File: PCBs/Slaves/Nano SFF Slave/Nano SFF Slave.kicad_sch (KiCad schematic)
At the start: 66 parts, among them J1 Screw_Terminal_01x02, J10 AVR-ISP-6, J11 Conn_01x06_Female, J12 Screw_Terminal_01x02, J13 Screw_Terminal_01x02, J14 Screw_Terminal_01x02, J15 Screw_Terminal_01x02, J16 Screw_Terminal_01x02, J2 Screw_Terminal_01x02, J3 Screw_Terminal_01x02, J4 Screw_Terminal_01x02, J5 Screw_Terminal_01x02, J6 Screw_Terminal_01x02, J7 Screw_Terminal_01x02, J8 Screw_Terminal_01x02, J9 Screw_Terminal_01x02, SW1 SW_DIP_x02, SW2 SW_DIP_x02, SW3 SW_MEC_5E, U1 ATmega328P-AU, U10 TISP4240M3BJR-S, U2 MAX487ESA+T, U3 ULN2003A, U4 MAX487CPA+, U5 AMS1117-5.0, U6 HY15P03C2, U7 TBU-CA065-200-WH, U8 TBU-CA065-200-WH, U9 TISP4240M3BJR-S, Y1 Crystal_GND24

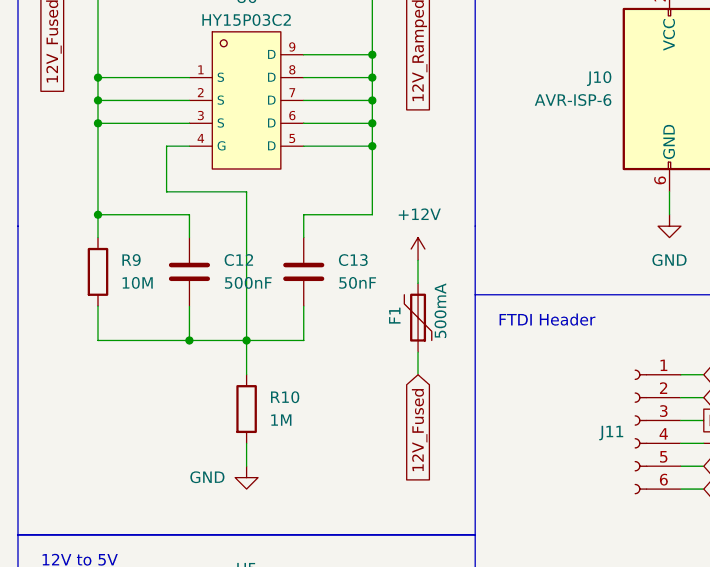
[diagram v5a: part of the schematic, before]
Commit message: Updated LCSC number and size of voltage ramp capacitors for Nano SFF Slave
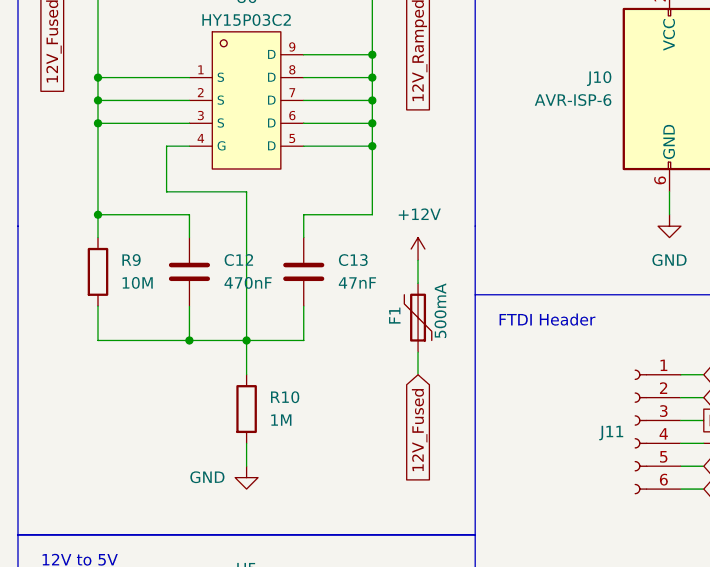
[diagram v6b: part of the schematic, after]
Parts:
- C12: value 500nF -> 470nF; footprint A10 KiCad Libraries:C0402 -> Capacitor_SMD:C_0603_1608Metric; LCSC TBA -> C1623
- C13: value 50nF -> 47nF; footprint A10 KiCad Libraries:C0402 -> Capacitor_SMD:C_0603_1608Metric; LCSC TBA -> C1622
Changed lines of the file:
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@@
       (effects (font (size 1.27 1.27)) (justify left))
     )
-    (property "Value" "50nF" (id 1) (at 48.26 95.2499 0)
-      (effects (font (size 1.27 1.27)) (justify left))
-    )
-    (property "Footprint" "A10 KiCad Libraries:C0402" (id 2) (at 45.4152 97.79 0)
+    (property "Value" "47nF" (id 1) (at 48.26 95.2499 0)
+      (effects (font (size 1.27 1.27)) (justify left))
+    )
+    (property "Footprint" "Capacitor_SMD:C_0603_1608Metric" (id 2) (at 45.4152 97.79 0)
       (effects (font (size 1.27 1.27)) hide)
     )
@@
       (effects (font (size 1.27 1.27)) hide)
     )
-    (property "LCSC" "TBA" (id 4) (at 44.45 93.98 0)
+    (property "LCSC" "C1622" (id 4) (at 44.45 93.98 0)
       (effects (font (size 1.27 1.27)) hide)
     )
@@
       (effects (font (size 1.27 1.27)) (justify left))
     )
-    (property "Value" "500nF" (id 1) (at 35.56 95.2499 0)
-      (effects (font (size 1.27 1.27)) (justify left))
-    )
-    (property "Footprint" "A10 KiCad Libraries:C0402" (id 2) (at 32.7152 97.79 0)
+    (property "Value" "470nF" (id 1) (at 35.56 95.2499 0)
+      (effects (font (size 1.27 1.27)) (justify left))
+    )
+    (property "Footprint" "Capacitor_SMD:C_0603_1608Metric" (id 2) (at 32.7152 97.79 0)
       (effects (font (size 1.27 1.27)) hide)
     )
@@
       (effects (font (size 1.27 1.27)) hide)
     )
-    (property "LCSC" "TBA" (id 4) (at 31.75 93.98 0)
+    (property "LCSC" "C1623" (id 4) (at 31.75 93.98 0)
       (effects (font (size 1.27 1.27)) hide)
     )
@@
     )
     (path "/dbc5fd48-5195-4b41-be0e-503a8df5dd8e"
-      (reference "C12") (unit 1) (value "500nF") (footprint "A10 KiCad Libraries:C0402")
+      (reference "C12") (unit 1) (value "470nF") (footprint "Capacitor_SMD:C_0603_1608Metric")
     )
     (path "/6e1cc3a1-d156-439d-9e01-aa13697bc266"
-      (reference "C13") (unit 1) (value "50nF") (footprint "A10 KiCad Libraries:C0402")
+      (reference "C13") (unit 1) (value "47nF") (footprint "Capacitor_SMD:C_0603_1608Metric")
     )
     (path "/294162e1-5bbc-43c1-8530-fdc705d0d68f"

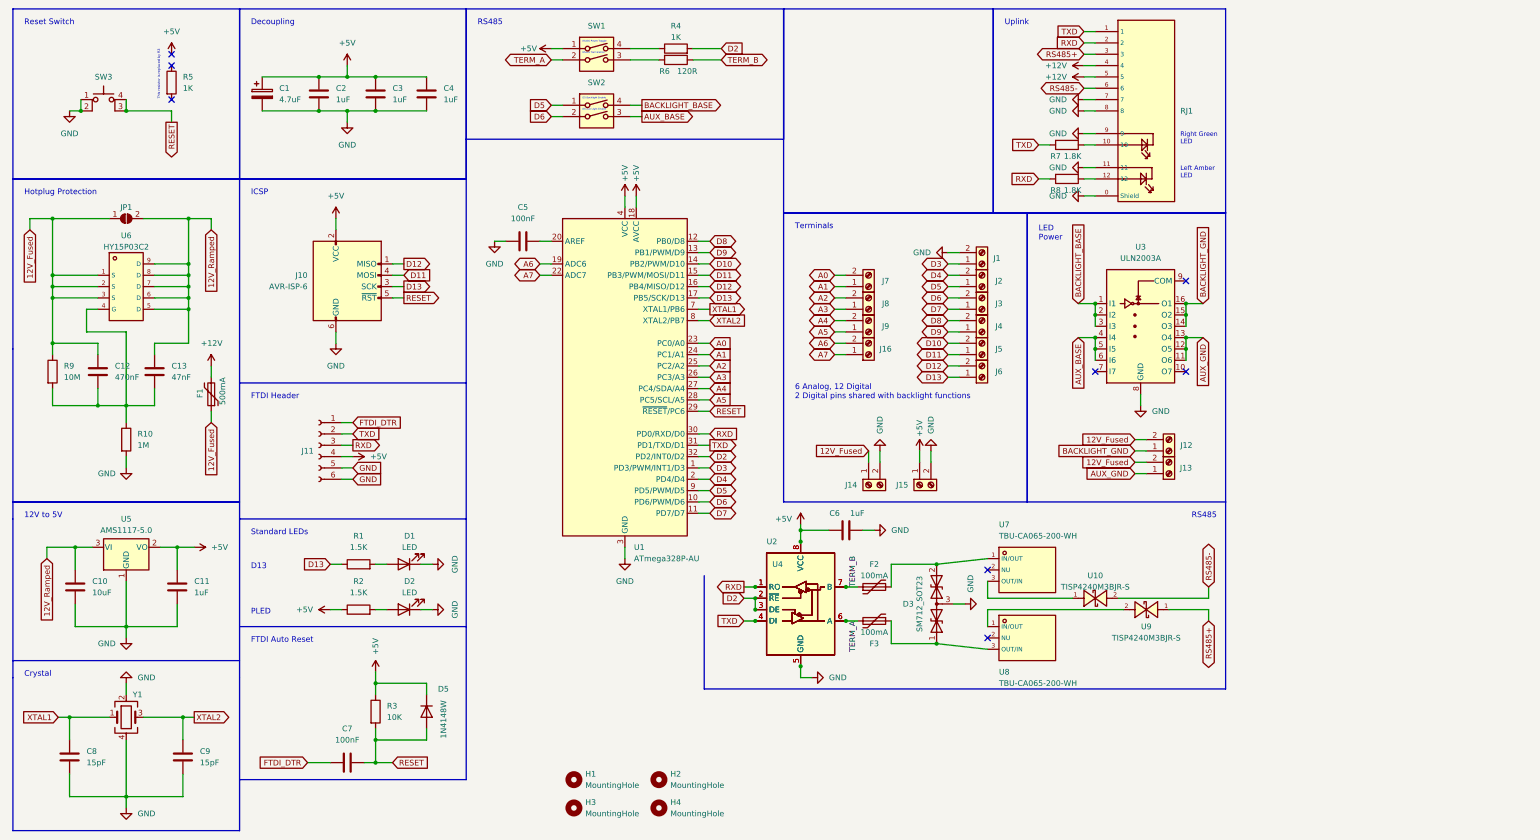
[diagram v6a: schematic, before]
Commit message: Removed voltage ramp and some protection from Nano SFF Slave
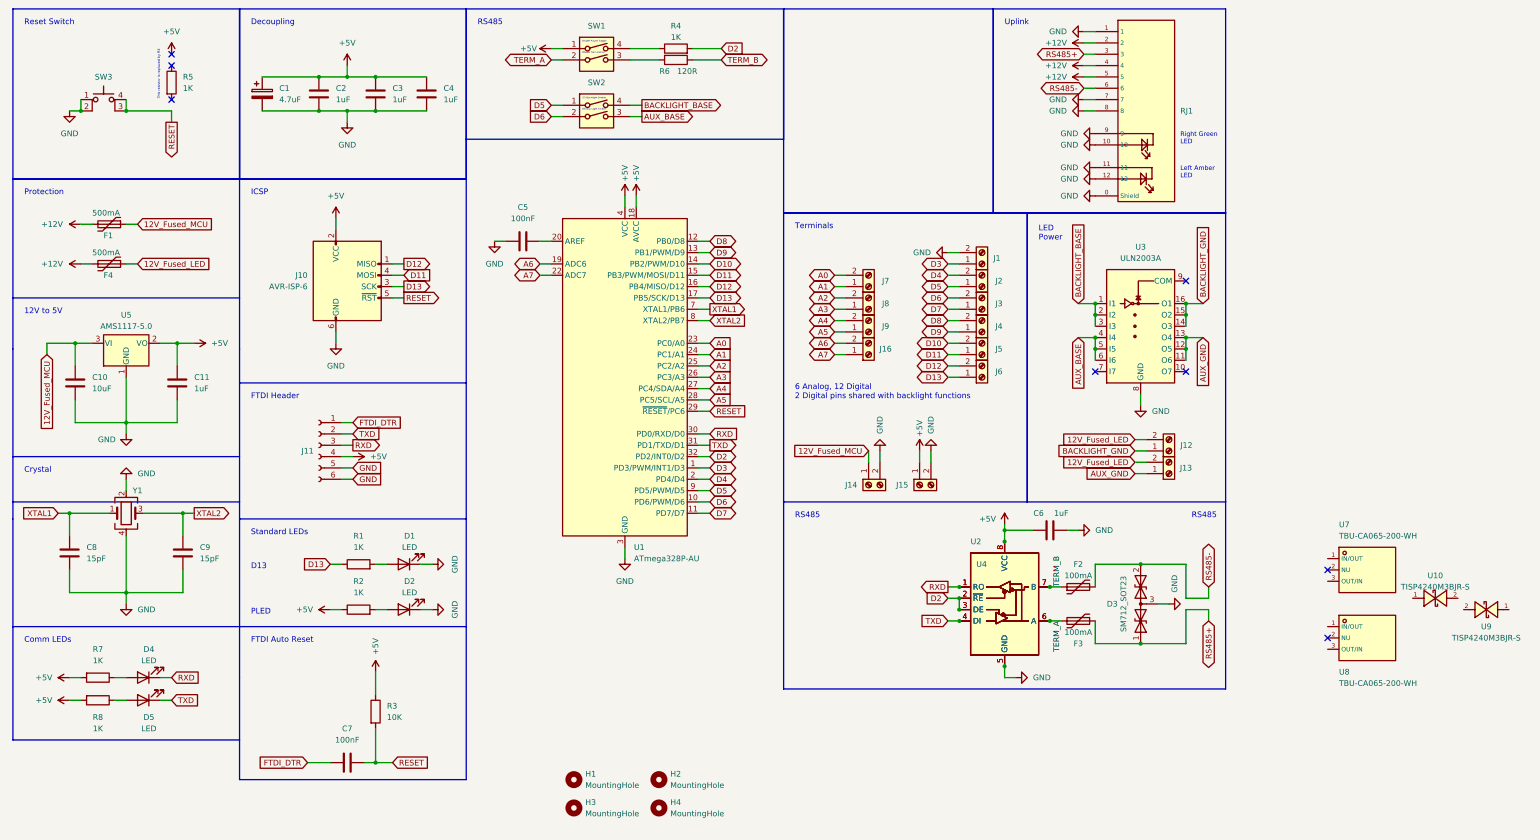
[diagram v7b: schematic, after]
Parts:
- removed C12: 470nF, Capacitor_SMD:C_0603_1608Metric, symbol Device:C
- removed C13: 47nF, Capacitor_SMD:C_0603_1608Metric, symbol Device:C
- removed D5: 1N4148W, Diode_SMD:D_SOD-123, symbol Device:D
- removed JP1: Solder, Jumper:SolderJumper-2_P1.3mm_Open_RoundedPad1.0x1.5mm, symbol Jumper:SolderJumper_2_Open
- removed R10: 1M, Resistor_SMD:R_0603_1608Metric, symbol Device:R
- removed R9: 10M, Resistor_SMD:R_0603_1608Metric, symbol Device:R
- removed U6: HY15P03C2, A10 KiCad Libraries:DFN-8_L5.9-W5.2-P1.27-LS6.2-BL, symbol A10:HY15P03C2
- added D4, D5: LED, LED_SMD:LED_0603_1608Metric, symbol Device:LED
- added F4: 500mA, Fuse:Fuse_1206_3216Metric, symbol Device:Polyfuse
- R1, R2: value 1.5K -> 1K; footprint Resistor_SMD:R_0805_2012Metric -> Resistor_SMD:R_0402_1005Metric; LCSC C4310 -> C11702
- R4: footprint Resistor_SMD:R_0805_2012Metric -> Resistor_SMD:R_0402_1005Metric; LCSC C17513 -> C11702
- R7, R8: value 1.8K -> 1K; footprint Resistor_SMD:R_0805_2012Metric -> Resistor_SMD:R_0402_1005Metric; LCSC C17398 -> C11702
- U10, U7, U8, U9: now left out of the parts list
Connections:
- net +12V: now also RJ1.2, F4.2
- net +5V: now also R7.2, R8.2
- net GND: now also RJ1.1, RJ1.10, RJ1.12
- net RS485+: now also D3.1 (A1), F3.1; no longer U9.1 (A)
- net RS485-: now also D3.2 (A2), F2.2; no longer U10.2 (K)
- net RXD: now also D4.1 (K); no longer R8.2, RJ1.2
- net TXD: now also D5.1 (K); no longer R7.2, RJ1.1
- net at U9.2 (K): no longer U8.1 (IN/OUT)
- net at U10.1 (A): no longer U7.3 (OUT/IN)
- net at R7.1: now also D4.2 (A); no longer RJ1.10
- net at R8.1: now also D5.2 (A); no longer RJ1.12
- net 12V_Fused renamed 12V_Fused_LED
- net 12V_Fused_LED: now also F4.1; no longer F1.1, J14.1 (Pin_1)
- net 12V_Ramped renamed 12V_Fused_MCU
- net 12V_Fused_MCU: now also F1.1, J14.1 (Pin_1)
- now unconnected: U7.1 (IN/OUT), U8.3 (OUT/IN)
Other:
- note added: "Comm LEDs"
- note added: "Protection"
- note removed: "Hotplug Protection"
- moved on the sheet: C10, C11, C6, C8, C9, D3, F1, F2, F3, U10, U2, U4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

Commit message: Updated Nano SFF Slave
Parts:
- added R10: 3.6K, Resistor_SMD:R_0603_1608Metric, symbol Device:R
- added R9: 1K, Resistor_SMD:R_0402_1005Metric, symbol Device:R
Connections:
- net +5V: now also R9.1
- net 12V_Fused_MCU: now also R10.1
- net GND: no longer RJ1.10, RJ1.12
- new net: R9.2, RJ1.10
- new net: R10.2, RJ1.12
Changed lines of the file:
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@@
     (stroke (width 0) (type default) (color 0 0 0 0))
   )
+  (wire (pts (xy 236.22 50.8) (xy 245.11 50.8))
+    (stroke (width 0) (type default) (color 0 0 0 0))
+  )
   (wire (pts (xy 196.85 82.55) (xy 199.39 82.55))
     (stroke (width 0) (type default) (color 0 0 0 0))
@@
     (stroke (width 0) (type default) (color 0 0 0 0))
   )
+  (wire (pts (xy 252.73 50.8) (xy 255.27 50.8))
+    (stroke (width 0) (type default) (color 0 0 0 0))
+  )
   (wire (pts (xy 25.4 125.73) (xy 25.4 130.81))
     (stroke (width 0) (type default) (color 0 0 0 0))
@@
     (stroke (width 0) (type default) (color 0 0 0 0))
   )
+  (wire (pts (xy 242.57 43.18) (xy 245.11 43.18))
+    (stroke (width 0) (type default) (color 0 0 0 0))
+  )
   (wire (pts (xy 222.25 149.86) (xy 224.79 149.86))
     (stroke (width 0) (type default) (color 0 0 0 0))
@@
     (stroke (width 0) (type default) (color 0 0 0 0))
   )
+  (wire (pts (xy 252.73 43.18) (xy 255.27 43.18))
+    (stroke (width 0) (type default) (color 0 0 0 0))
+  )
   (wire (pts (xy 38.1 33.02) (xy 38.1 35.56))
     (stroke (width 0) (type default) (color 0 0 0 0))
@@
     )
   )
+  (global_label "12V_Fused_MCU" (shape input) (at 236.22 50.8 90) (fields_autoplaced)
+    (effects (font (size 1.27 1.27)) (justify left))
+    (property "Intersheet References" "${INTERSHEET_REFS}" (id 0) (at 236.2994 33.3888 90)
+      (effects (font (size 1.27 1.27)) (justify left) hide)
+    )
+  )
   (global_label "12V_Fused_LED" (shape input) (at 264.16 109.22 180) (fields_autoplaced)
     (effects (font (size 1.27 1.27)) (justify right))
@@
   )
   (symbol (lib_id "power:GND") (at 255.27 54.61 270) (unit 1)
-    (in_bom yes) (on_board yes) (fields_autoplaced)
+    (in_bom yes) (on_board yes)
     (property "Reference" "#PWR0118" (id 0) (at 248.92 54.61 0)
       (effects (font (size 1.27 1.27)) hide)
     )
-    (property "Value" "GND" (id 1) (at 251.46 54.6099 90)
+    (property "Value" "GND" (id 1) (at 251.46 55.88 90)
       (effects (font (size 1.27 1.27)) (justify right))
     )
@@
   (symbol (lib_id "power:GND") (at 255.27 40.64 270) (unit 1)
     (in_bom yes) (on_board yes) (fields_autoplaced)
-    (property "Reference" "#PWR?" (id 0) (at 248.92 40.64 0)
+    (property "Reference" "#PWR0121" (id 0) (at 248.92 40.64 0)
       (effects (font (size 1.27 1.27)) hide)
     )
@@
     (pin "1")
   )
+  (symbol (lib_id "Device:R") (at 248.92 43.18 90) (unit 1)
+    (in_bom yes) (on_board yes)
+    (property "Reference" "R9" (id 0) (at 246.38 45.72 90))
+    (property "Value" "1K" (id 1) (at 251.46 45.72 90))
+    (property "Footprint" "Resistor_SMD:R_0402_1005Metric" (id 2) (at 248.92 44.958 90)
+      (effects (font (size 1.27 1.27)) hide)
+    )
+    (property "Datasheet" "~" (id 3) (at 248.92 43.18 0)
+      (effects (font (size 1.27 1.27)) hide)
+    )
+    (property "LCSC" "C11702" (id 4) (at 248.92 43.18 0)
+      (effects (font (size 1.27 1.27)) hide)
+    )
+    (pin "1")
+    (pin "2")
+  )
   (symbol (lib_id "Connector:Screw_Terminal_01x02") (at 229.87 90.17 0) (mirror x) (unit 1)
     (in_bom yes) (on_board yes)
@@
   (symbol (lib_id "power:GND") (at 255.27 48.26 270) (unit 1)
     (in_bom yes) (on_board yes) (fields_autoplaced)
-    (property "Reference" "#PWR?" (id 0) (at 248.92 48.26 0)
+    (property "Reference" "#PWR0130" (id 0) (at 248.92 48.26 0)
       (effects (font (size 1.27 1.27)) hide)
     )
@@
     (pin "2")
   )
-  (symbol (lib_id "power:GND") (at 255.27 50.8 270) (unit 1)
-    (in_bom yes) (on_board yes) (fields_autoplaced)
-    (property "Reference" "#PWR?" (id 0) (at 248.92 50.8 0)
-      (effects (font (size 1.27 1.27)) hide)
-    )
-    (property "Value" "GND" (id 1) (at 251.46 50.7999 90)
-      (effects (font (size 1.27 1.27)) (justify right))
-    )
-    (property "Footprint" "" (id 2) (at 255.27 50.8 0)
-      (effects (font (size 1.27 1.27)) hide)
-    )
-    (property "Datasheet" "" (id 3) (at 255.27 50.8 0)
-      (effects (font (size 1.27 1.27)) hide)
-    )
-    (pin "1")
-  )
   (symbol (lib_id "power:GND") (at 85.09 87.63 0) (unit 1)
     (in_bom yes) (on_board yes)
@@
     (pin "1")
   )
-  (symbol (lib_id "power:GND") (at 255.27 43.18 270) (unit 1)
-    (in_bom yes) (on_board yes) (fields_autoplaced)
-    (property "Reference" "#PWR?" (id 0) (at 248.92 43.18 0)
+  (symbol (lib_id "Device:R") (at 248.92 50.8 90) (unit 1)
+    (in_bom yes) (on_board yes)
+    (property "Reference" "R10" (id 0) (at 246.38 53.34 90))
+    (property "Value" "3.6K" (id 1) (at 251.46 53.34 90))
+    (property "Footprint" "Resistor_SMD:R_0603_1608Metric" (id 2) (at 248.92 52.578 90)
       (effects (font (size 1.27 1.27)) hide)
     )
-    (property "Value" "GND" (id 1) (at 251.46 43.1799 90)
-      (effects (font (size 1.27 1.27)) (justify right))
-    )
-    (property "Footprint" "" (id 2) (at 255.27 43.18 0)
+    (property "Datasheet" "~" (id 3) (at 248.92 50.8 0)
       (effects (font (size 1.27 1.27)) hide)
     )
-    (property "Datasheet" "" (id 3) (at 255.27 43.18 0)
+    (property "LCSC" "C22980" (id 4) (at 248.92 50.8 0)
       (effects (font (size 1.27 1.27)) hide)
     )
     (pin "1")
+    (pin "2")
   )
   (symbol (lib_id "power:+5V") (at 93.98 161.29 0) (unit 1)
@@
     (pin "4")
   )
+  (symbol (lib_id "power:+5V") (at 242.57 43.18 90) (unit 1)
+    (in_bom yes) (on_board yes)
+    (property "Reference" "#PWR0126" (id 0) (at 246.38 43.18 0)
+      (effects (font (size 1.27 1.27)) hide)
+    )
+    (property "Value" "+5V" (id 1) (at 243.84 45.72 90)
+      (effects (font (size 1.27 1.27)) (justify left))
+    )
+    (property "Footprint" "" (id 2) (at 242.57 43.18 0)
+      (effects (font (size 1.27 1.27)) hide)
+    )
+    (property "Datasheet" "" (id 3) (at 242.57 43.18 0)
+      (effects (font (size 1.27 1.27)) hide)
+    )
+    (pin "1")
+  )
   (symbol (lib_id "Connector:Screw_Terminal_01x02") (at 215.9 119.38 90) (mirror x) (unit 1)
     (in_bom yes) (on_board yes)
@@
       (reference "#PWR0120") (unit 1) (value "GND") (footprint "")
     )
+    (path "/4a0c185c-d332-4d31-a687-f91324a5a494"
+      (reference "#PWR0121") (unit 1) (value "GND") (footprint "")
+    )
     (path "/e70032e1-593f-4b8c-9b9c-ad55a3745622"
       (reference "#PWR0122") (unit 1) (value "GND") (footprint "")
@@
       (reference "#PWR0125") (unit 1) (value "+5V") (footprint "")
     )
+    (path "/f12cc227-a1c5-4cc6-bc92-a3276fd7ae08"
+      (reference "#PWR0126") (unit 1) (value "+5V") (footprint "")
+    )
     (path "/8537ef08-22e1-4eec-a09a-d58a3e6da0d2"
       (reference "#PWR0127") (unit 1) (value "+5V") (footprint "")
@@
       (reference "#PWR0129") (unit 1) (value "GND") (footprint "")
     )
+    (path "/6f4643bb-52e5-447e-8449-b8bc3d86b2e0"
+      (reference "#PWR0130") (unit 1) (value "GND") (footprint "")
+    )
     (path "/a94de019-f56e-4619-9189-74d5a7cc128f"
       (reference "#PWR0131") (unit 1) (value "+12V") (footprint "")
@@
       (reference "#PWR0145") (unit 1) (value "+5V") (footprint "")
     )
-    (path "/4a0c185c-d332-4d31-a687-f91324a5a494"
-      (reference "#PWR?") (unit 1) (value "GND") (footprint "")
-    )
-    (path "/6f4643bb-52e5-447e-8449-b8bc3d86b2e0"
-      (reference "#PWR?") (unit 1) (value "GND") (footprint "")
-    )
-    (path "/c16051de-397b-43f7-8128-62b490be7cfc"
-      (reference "#PWR?") (unit 1) (value "GND") (footprint "")
-    )
-    (path "/d054fe41-3500-4ef5-9852-f7fb7b1bea14"
-      (reference "#PWR?") (unit 1) (value "GND") (footprint "")
-    )
     (path "/df5accf7-095f-40f9-b40a-a9b9e4c1a11a"
       (reference "C1") (unit 1) (value "4.7uF") (footprint "A10 KiCad Libraries:C0805")
@@
       (reference "R8") (unit 1) (value "1K") (footprint "Resistor_SMD:R_0402_1005Metric")
     )
+    (path "/67afc716-6f62-4185-8366-23dd26605e5b"
+      (reference "R9") (unit 1) (value "1K") (footprint "Resistor_SMD:R_0402_1005Metric")
+    )
+    (path "/cef69c45-d1b9-4ad8-a826-d9e3e591eaf5"
+      (reference "R10") (unit 1) (value "3.6K") (footprint "Resistor_SMD:R_0603_1608Metric")
+    )
     (path "/b0d080a8-fb27-4ca9-906d-778ef01ddc29"
